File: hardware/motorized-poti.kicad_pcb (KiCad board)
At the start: 2 copper layers, 100 x 20 mm, 31 parts, among them J1 AKL_5_2, P1 CON-SENSOR2, P2 MOTORIZED_POTI, P3 BOOT, P4 CONN_02X04, P5 CONN_02X04, U1 XMC1XXX24, U2 ZXBM5210, U3 DRILL, U4 DRILL, U5 DRILL, U6 DRILL

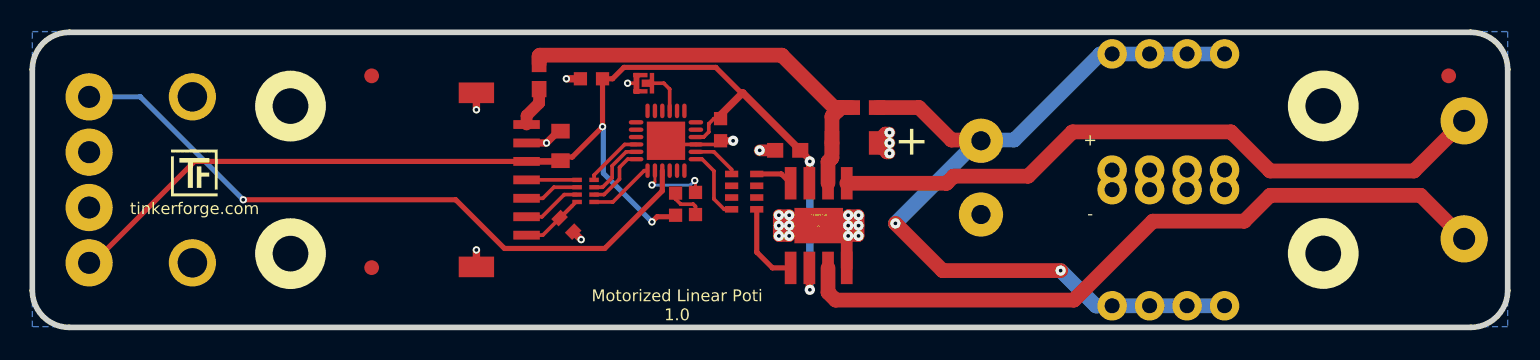
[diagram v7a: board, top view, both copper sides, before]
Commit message: fix mounting hole position, change wire angle
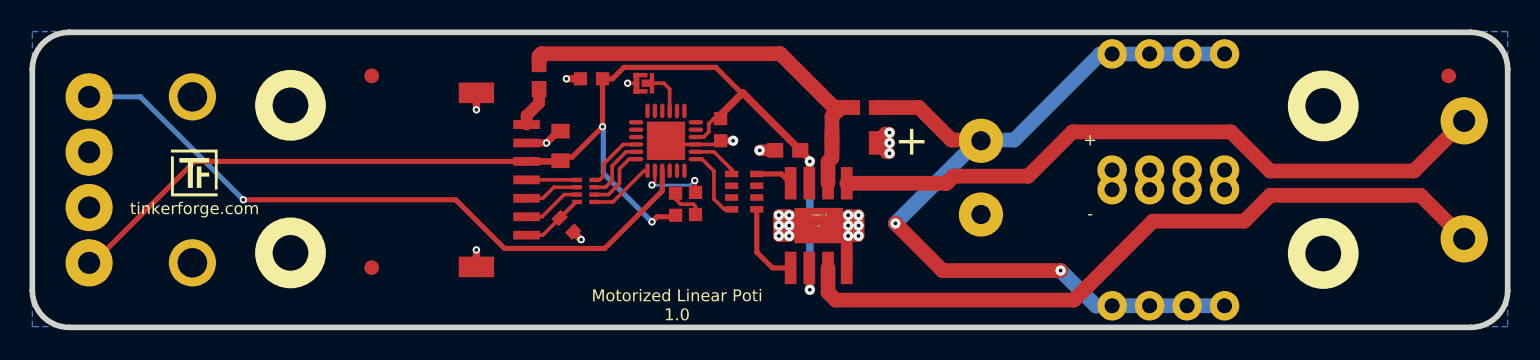
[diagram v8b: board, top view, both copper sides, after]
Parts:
- moved U3 0.05 mm to (95.1, 95.6)
- moved U4 0.05 mm to (95.1, 105.6)
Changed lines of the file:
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@@
-(kicad_pcb (version 4) (host pcbnew 4.0.2+dfsg1-stable)
+(kicad_pcb (version 4) (host pcbnew 4.0.6-e0-6349~53~ubuntu16.04.1)
   (general
     (links 70)
     (no_connects 0)
-    (area 77.409499 90.459499 177.790501 110.840501)
+    (area 70.875139 90.459499 282.795857 162.890793)
     (thickness 1.6002)
     (drawings 14)
-    (tracks 235)
+    (tracks 237)
     (zones 0)
     (modules 31)
@@
     (aux_axis_origin 77.6 90.6)
     (grid_origin 77.6 90.6)
-    (visible_elements FFFFFF3F)
+    (visible_elements FFFF7F3F)
     (pcbplotparams
       (layerselection 0x00030_80000001)
@@
   )
   (module kicad-libraries:DRILL_NP (layer Vorderseite)
-    (at 95.1 95.65 270)
+    (at 95.1 95.6 270)
     (fp_text reference U3 (at 0 0 270) (layer F.SilkS) hide
       (effects (font (size 0.29972 0.29972) (thickness 0.0762)))
@@
   )
   (module kicad-libraries:DRILL_NP (layer Vorderseite)
-    (at 95.1 105.65 90)
+    (at 95.1 105.6 90)
     (fp_text reference U4 (at 0 0 90) (layer F.SilkS) hide
       (effects (font (size 0.29972 0.29972) (thickness 0.0762)))
@@
   (segment (start 113.2001 99.4) (end 113.4 99.2001) (width 0.45) (layer Vorderseite) (net 8))
   (segment (start 111.95 92.7999) (end 111.95 92.25) (width 1.00076) (layer Vorderseite) (net 9))
-  (segment (start 111.95 92.25) (end 112 92.2) (width 1.00076) (layer Vorderseite) (net 9))
+  (segment (start 111.95 92.25) (end 112.1 92.1) (width 1.00076) (layer Vorderseite) (net 9))
   (segment (start 132.175 95.975) (end 132.175 95.75) (width 1.00076) (layer Vorderseite) (net 9))
-  (segment (start 128.4 92.2) (end 132.175 95.975) (width 1.00076) (layer Vorderseite) (net 9))
-  (segment (start 112 92.2) (end 128.4 92.2) (width 1.00076) (layer Vorderseite) (net 9))
+  (segment (start 128.3 92.1) (end 132.175 95.975) (width 1.00076) (layer Vorderseite) (net 9))
+  (segment (start 112.1 92.1) (end 128.3 92.1) (width 1.00076) (layer Vorderseite) (net 9))
   (segment (start 131.53246 100.88234) (end 131.53246 99.41754) (width 1.00076) (layer Vorderseite) (net 9))
   (segment (start 131.79886 99.15114) (end 131.79886 98.15) (width 1.00076) (layer Vorderseite) (net 9))
@@
   (segment (start 119.075 100.025) (end 119.3 100.025) (width 0.25) (layer Vorderseite) (net 10))
   (segment (start 116.9507 102.1493) (end 119.075 100.025) (width 0.25) (layer Vorderseite) (net 10))
-  (segment (start 115.675 101.64892) (end 116.35108 101.64892) (width 0.25) (layer Vorderseite) (net 11))
-  (segment (start 117.95 99.25) (end 118.525 99.25) (width 0.25) (layer Vorderseite) (net 11))
-  (segment (start 117.4 99.8) (end 117.95 99.25) (width 0.25) (layer Vorderseite) (net 11))
-  (segment (start 117.4 100.6) (end 117.4 99.8) (width 0.25) (layer Vorderseite) (net 11))
-  (segment (start 116.35108 101.64892) (end 117.4 100.6) (width 0.25) (layer Vorderseite) (net 11))
-  (segment (start 115.675 101.15108) (end 116.24892 101.15108) (width 0.25) (layer Vorderseite) (net 12))
+  (segment (start 115.675 101.64892) (end 116.65108 101.64892) (width 0.25) (layer Vorderseite) (net 11))
+  (segment (start 118.05 99.25) (end 118.525 99.25) (width 0.25) (layer Vorderseite) (net 11))
+  (segment (start 117.4 99.9) (end 118.05 99.25) (width 0.249) (layer Vorderseite) (net 11))
+  (segment (start 117.4 100.9) (end 117.4 99.9) (width 0.25) (layer Vorderseite) (net 11))
+  (segment (start 116.65108 101.64892) (end 117.4 100.9) (width 0.25) (layer Vorderseite) (net 11))
+  (segment (start 115.675 101.15108) (end 116.44892 101.15108) (width 0.25) (layer Vorderseite) (net 12))
   (segment (start 117.85 98.75) (end 118.525 98.75) (width 0.25) (layer Vorderseite) (net 12))
   (segment (start 116.9 99.7) (end 117.85 98.75) (width 0.25) (layer Vorderseite) (net 12))
-  (segment (start 116.9 100.5) (end 116.9 99.7) (width 0.25) (layer Vorderseite) (net 12))
-  (segment (start 116.24892 101.15108) (end 116.9 100.5) (width 0.25) (layer Vorderseite) (net 12))
-  (segment (start 115.675 100.6507) (end 115.675 100.325) (width 0.25) (layer Vorderseite) (net 13))
-  (segment (start 117.75 98.25) (end 118.525 98.25) (width 0.25) (layer Vorderseite) (net 13))
-  (segment (start 115.675 100.325) (end 117.75 98.25) (width 0.25) (layer Vorderseite) (net 13))
+  (segment (start 116.9 100.7) (end 116.9 99.7) (width 0.25) (layer Vorderseite) (net 12))
+  (segment (start 116.44892 101.15108) (end 116.9 100.7) (width 0.25) (layer Vorderseite) (net 12))
+  (segment (start 115.675 100.6507) (end 116.0493 100.6507) (width 0.249) (layer Vorderseite) (net 13))
+  (segment (start 116.3 100.4) (end 116.3 99.6) (width 0.249) (layer Vorderseite) (net 13))
+  (segment (start 116.0493 100.6507) (end 116.3 100.4) (width 0.249) (layer Vorderseite) (net 13))
+  (segment (start 117.65 98.25) (end 118.525 98.25) (width 0.25) (layer Vorderseite) (net 13))
+  (segment (start 116.3 99.6) (end 117.65 98.25) (width 0.25) (layer Vorderseite) (net 13))
   (segment (start 119.2 94.1) (end 119.6 94.1) (width 0.2) (layer Vorderseite) (net 14))
   (segment (start 119.2 94.1) (end 120.4 94.1) (width 0.25) (layer Vorderseite) (net 14))
@@
     (polygon
       (pts
-        (xy 177.6 110.6) (xy 77.6 110.6) (xy 77.6 90.6) (xy 177.6 90.6) (xy 177.6 110.6)
+        (xy 177.6 110.6) (xy 77.6 110.6) (xy 77.6 90.6) (xy 177.6 90.6)
       )
     )
